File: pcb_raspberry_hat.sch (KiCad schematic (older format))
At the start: 9 parts, among them P1 Conn_02x20_Odd_Even

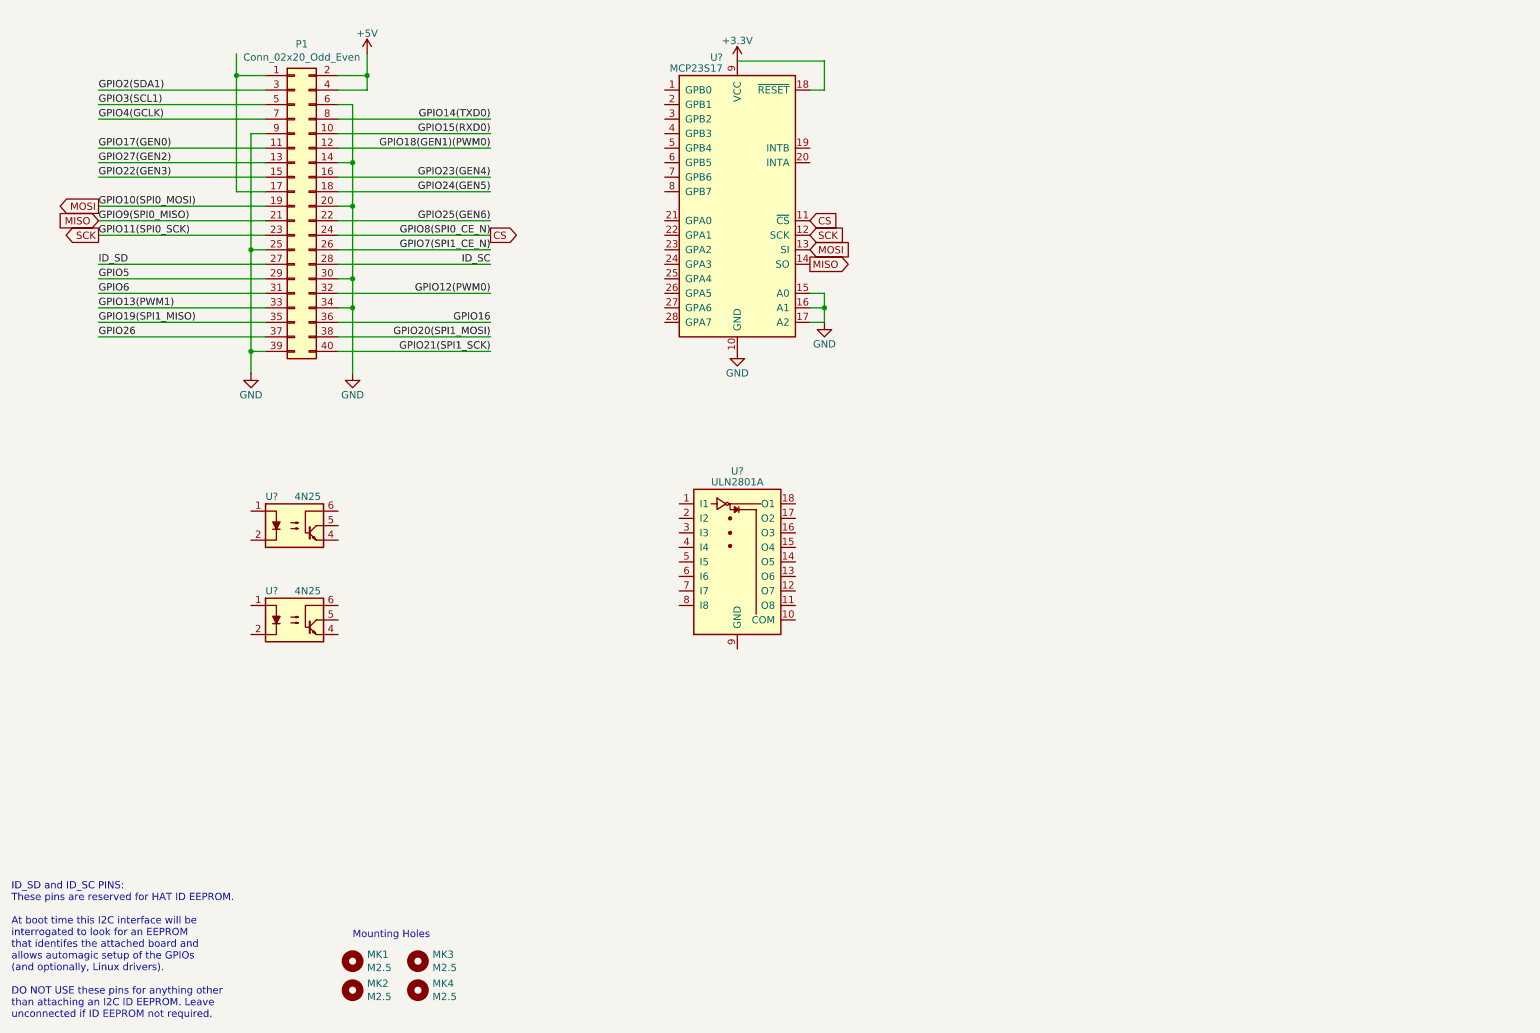
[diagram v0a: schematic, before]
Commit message: ESQUEMÁTICO
novas ligações no esquematico, 7seg adicionado, lcd nao implementado
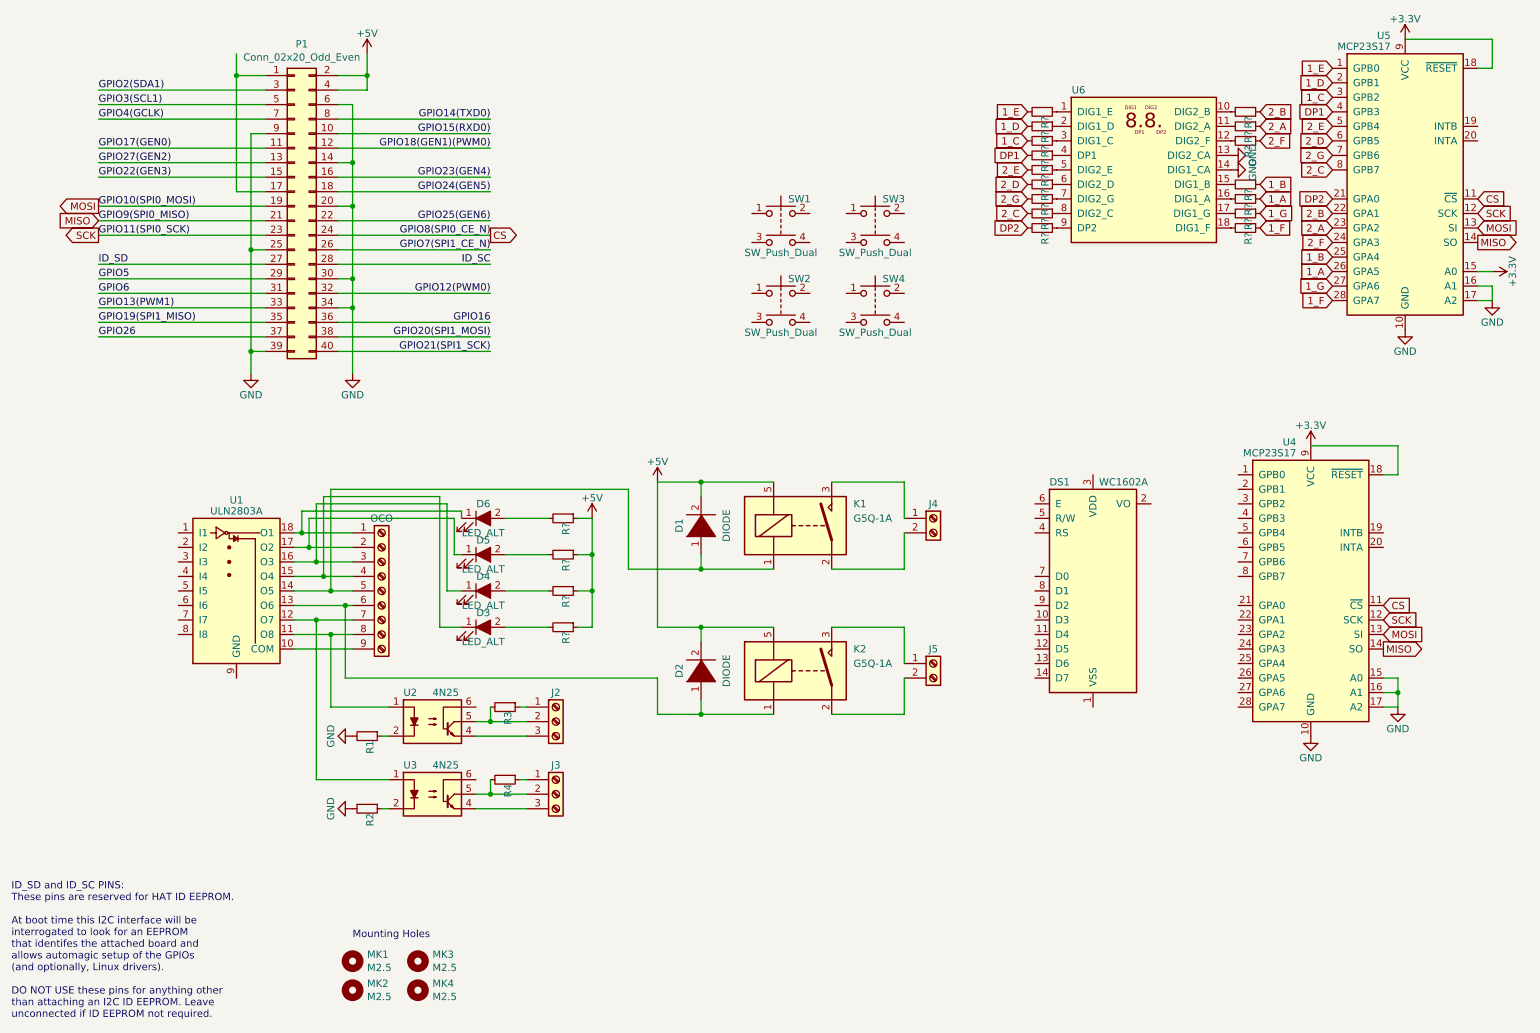
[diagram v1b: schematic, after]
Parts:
- removed U?: 4N25, Housings_DIP:DIP-6_W7.62mm, symbol 4N25
- removed U?: ULN2801A, symbol ULN2801A
- added D1, D2: DIODE, symbol DIODE
- added D3, D4, D5, D6: LED_ALT, symbol LED_ALT
- added DS1: WC1602A, Displays:WC1602A, symbol WC1602A
- added J2, J3: Screw_Terminal_01x03, symbol Screw_Terminal_01x03
- added J4, J5: Screw_Terminal_01x02, symbol Screw_Terminal_01x02
- added K1, K2: G5Q-1A, Relays_THT:Relay_SPST-NO_OMRON-G5Q, symbol G5Q-1A
- added OCO: Screw_Terminal_01x09, symbol Screw_Terminal_01x09
- added R1, R2, R3, R4, R? (x20): R_Small, symbol R_Small
- added SW1, SW2, SW3, SW4: SW_Push_Dual, symbol SW_Push_Dual
- added U1: ULN2803A, symbol ULN2803A
- added U2: 4N25, Housings_DIP:DIP-6_W7.62mm, symbol 4N25
- added U5: MCP23S17, symbol MCP23S17
- added U6: DA56-11CGKWA, Displays_7-Segment:DA56-11CGKWA, symbol DA56-11CGKWA
- gave numbers to parts that had none: 2
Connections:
- net +3V3: now also U5.15 (A0), U5.18 (~RESET), U5.9 (VCC)
- net +5V: now also D1.2 (A), D2.2 (A), K1.5, K2.5, R?.1, R?.1, R?.1, R?.1
- net CS: now also U5.11 (~CS)
- net GND: now also R1.2, R2.2, U5.10 (GND), U5.16 (A1), U5.17 (A2), U6.13 (DIG2_CA), U6.14 (DIG1_CA)
- net MISO: now also U5.14 (SO)
- net MOSI: now also U5.13 (SI)
- net SCK: now also U5.12 (SCK)
- net at U3.1: now also OCO.7 (Pin_7), U1.12 (O7)
- net at U3.2: now also R2.1
- net at U3.4: now also J3.3 (Pin_3)
- net at U3.5: now also J3.2 (Pin_2), R4.2
- new net: D1.1 (K), K1.1, OCO.5 (Pin_5), U1.14 (O5)
- new net: J4.2 (Pin_2), K1.2
- new net: J4.1 (Pin_1), K1.3
- new net: D2.1 (K), K2.1, OCO.6 (Pin_6), U1.13 (O6)
- new net: J5.2 (Pin_2), K2.2
- new net: J5.1 (Pin_1), K2.3
- new net: OCO.9 (Pin_9), U1.10 (COM)
- new net: OCO.8 (Pin_8), U1.11 (O8), U2.1
- new net: D3.1 (K), OCO.4 (Pin_4), U1.15 (O4)
- new net: D4.1 (K), OCO.3 (Pin_3), U1.16 (O3)
- new net: D5.1 (K), OCO.2 (Pin_2), U1.17 (O2)
- new net: D6.1 (K), OCO.1 (Pin_1), U1.18 (O1)
- new net: D3.2 (A), R?.2
- new net: D4.2 (A), R?.2
- new net: D5.2 (A), R?.2
- new net: D6.2 (A), R?.2
- new net: R?.1, U6.1 (DIG1_E)
- new net: R?.2, U6.10 (DIG2_B)
- new net: R?.2, U6.11 (DIG2_A)
- new net: R?.2, U6.12 (DIG2_F)
- new net: R?.2, U6.15 (DIG1_B)
- new net: R?.2, U6.16 (DIG1_A)
- new net: R?.2, U6.17 (DIG1_G)
- new net: R?.2, U6.18 (DIG1_F)
- new net: R?.1, U6.2 (DIG1_D)
- new net: R?.1, U6.3 (DIG1_C)
- new net: R?.1, U6.4 (DP1)
- new net: R?.1, U6.5 (DIG2_E)
- new net: R?.1, U6.6 (DIG2_D)
- new net: R?.1, U6.7 (DIG2_G)
- new net: R?.1, U6.8 (DIG2_C)
- new net: R?.1, U6.9 (DP2)
- new net: J3.1 (Pin_1), R4.1
- new net: R1.1, U2.2
- new net: J2.3 (Pin_3), U2.4
- new net: J2.2 (Pin_2), R3.2, U2.5
- new net: J2.1 (Pin_1), R3.1
- new net 1_A: R?.1, U5.26 (GPA5)
- new net 1_B: R?.1, U5.25 (GPA4)
- new net 1_C: R?.2, U5.3 (GPB2)
- new net 1_D: R?.2, U5.2 (GPB1)
- new net 1_E: R?.2, U5.1 (GPB0)
- new net 1_F: R?.1, U5.28 (GPA7)
- new net 1_G: R?.1, U5.27 (GPA6)
- new net 2_A: R?.1, U5.23 (GPA2)
- new net 2_B: R?.1, U5.22 (GPA1)
- new net 2_C: R?.2, U5.8 (GPB7)
- new net 2_D: R?.2, U5.6 (GPB5)
- new net 2_E: R?.2, U5.5 (GPB4)
- new net 2_F: R?.1, U5.24 (GPA3)
- new net 2_G: R?.2, U5.7 (GPB6)
- new net DP1: R?.2, U5.4 (GPB3)
- new net DP2: R?.2, U5.21 (GPA0)
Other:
- moved on the sheet: U3, U4
